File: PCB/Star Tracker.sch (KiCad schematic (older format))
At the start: 29 parts

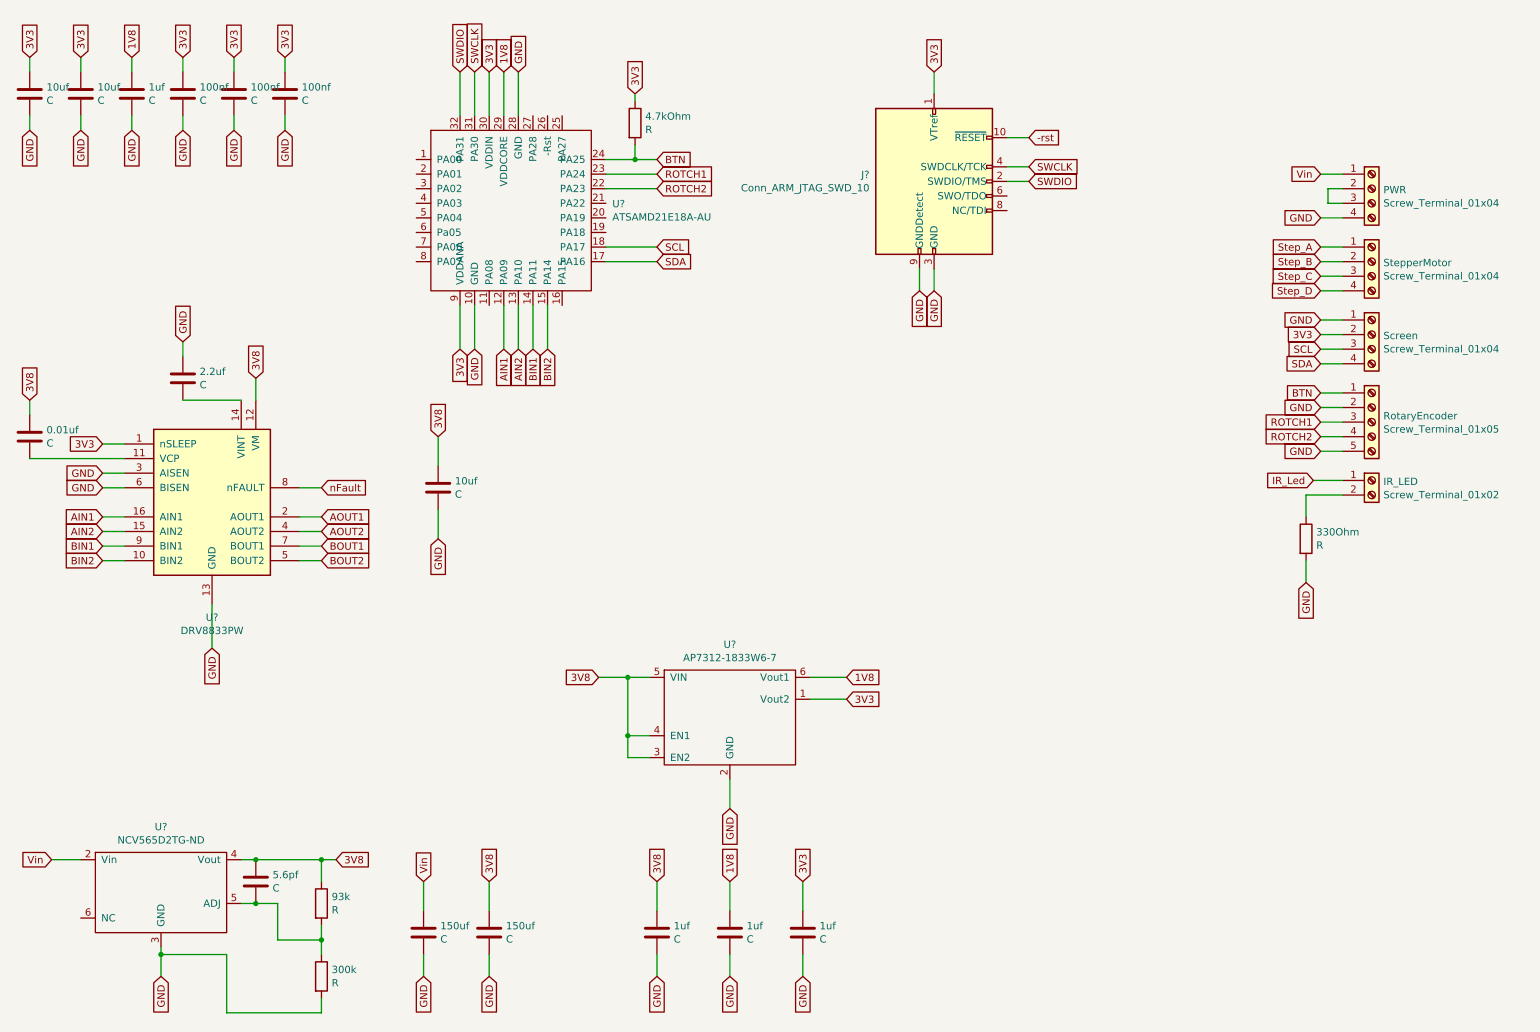
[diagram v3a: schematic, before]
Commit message: Fixed broken schematic and started on layout
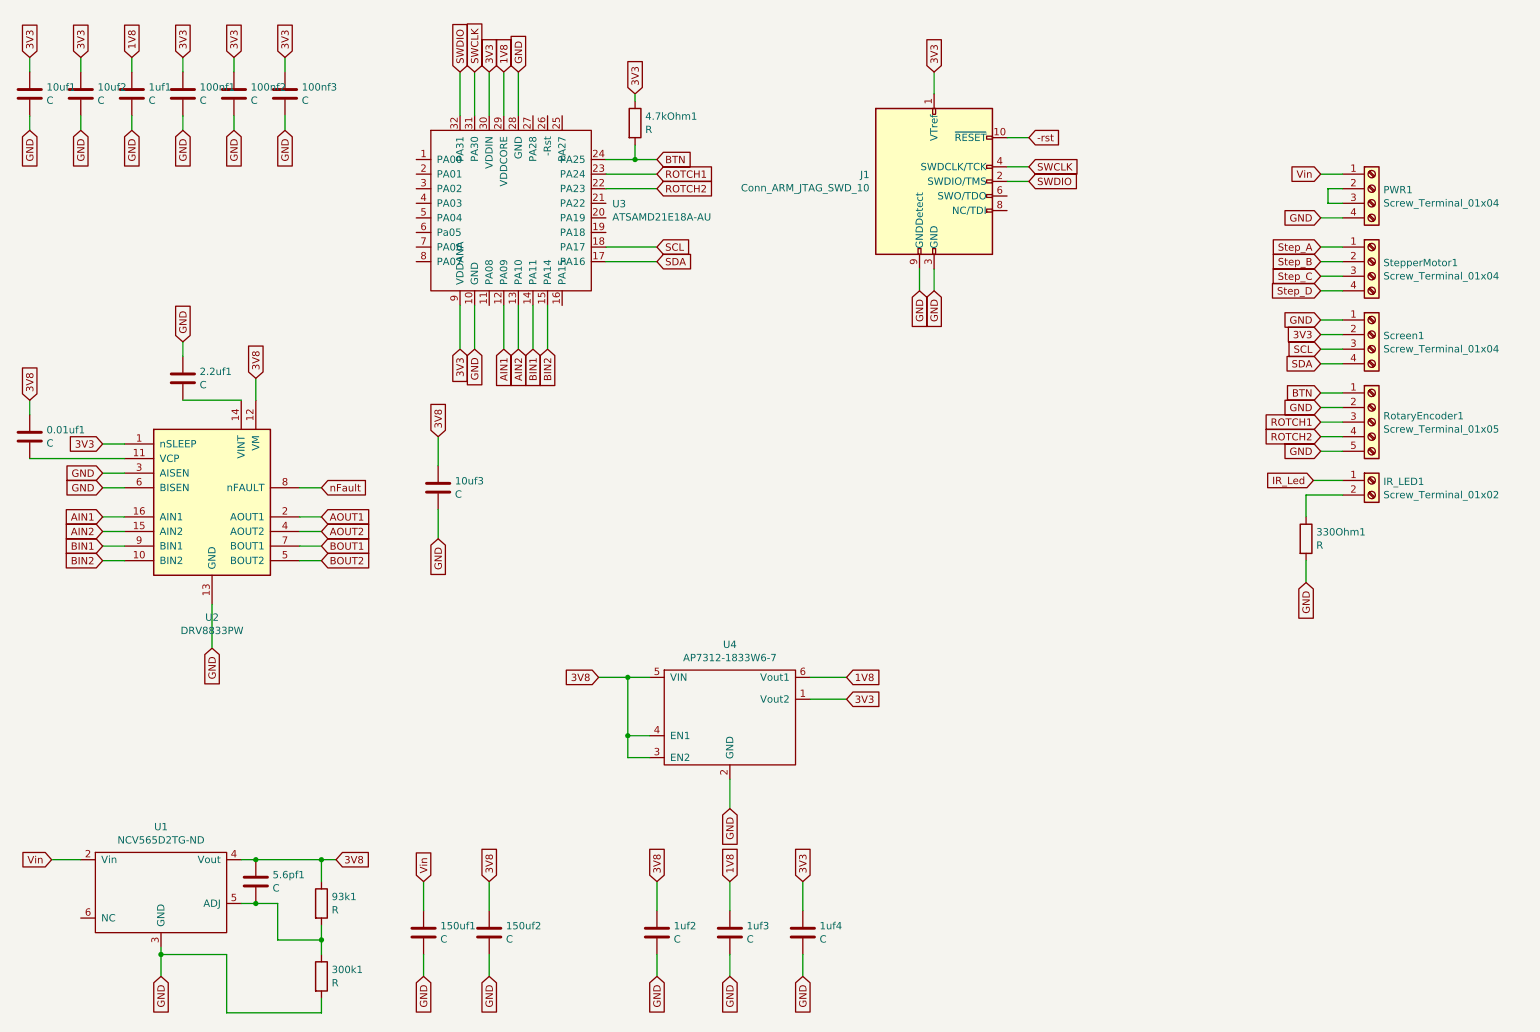
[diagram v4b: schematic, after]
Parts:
- 0.01uf1: renamed from 0.01uf; footprint (none) -> Capacitor_SMD:C_1206_3216Metric
- 100nf1, 100nf2, 100nf3: renamed from 100nf; footprint (none) -> Capacitor_SMD:C_1206_3216Metric
- 10uf1, 10uf2, 10uf3: renamed from 10uf; footprint (none) -> Capacitor_SMD:C_1206_3216Metric
- 150uf1, 150uf2: renamed from 150uf; footprint (none) -> Capacitor_SMD:C_1206_3216Metric
- 1uf1, 1uf2, 1uf3, 1uf4: renamed from 1uf; footprint (none) -> Capacitor_SMD:C_1206_3216Metric
- 2.2uf1: renamed from 2.2uf; footprint (none) -> Capacitor_SMD:C_1206_3216Metric
- 300k1: renamed from 300k; footprint (none) -> Resistor_SMD:R_1206_3216Metric
- 330Ohm1: renamed from 330Ohm; footprint (none) -> Resistor_SMD:R_1206_3216Metric
- 4.7kOhm1: renamed from 4.7kOhm; footprint (none) -> Resistor_SMD:R_1206_3216Metric
- 5.6pf1: renamed from 5.6pf; footprint (none) -> Capacitor_SMD:C_1206_3216Metric
- 93k1: renamed from 93k; footprint (none) -> Resistor_SMD:R_1206_3216Metric
- IR_LED1: renamed from IR_LED; footprint (none) -> Connector_Phoenix_MC:PhoenixContact_MC_1,5_2-G-3.5_1x02_P3.50mm_Horizontal
- J1: renamed from J?; footprint (none) -> Connector_PinHeader_1.27mm:PinHeader_2x05_P1.27mm_Vertical_SMD
- PWR1: renamed from PWR; footprint (none) -> Connector_Phoenix_MC:PhoenixContact_MC_1,5_4-G-3.5_1x04_P3.50mm_Horizontal
- RotaryEncoder1: renamed from RotaryEncoder; footprint (none) -> Connector_Phoenix_MC:PhoenixContact_MC_1,5_5-G-3.5_1x05_P3.50mm_Horizontal
- Screen1: renamed from Screen; footprint (none) -> Connector_Phoenix_MC:PhoenixContact_MC_1,5_4-G-3.5_1x04_P3.50mm_Horizontal
- StepperMotor1: renamed from StepperMotor; footprint (none) -> Connector_Phoenix_MC:PhoenixContact_MC_1,5_4-G-3.5_1x04_P3.50mm_Horizontal
- U1: renamed from U?; footprint (none) -> Package_TO_SOT_SMD:TO-263-5_TabPin6
- U3: renamed from U?; footprint (none) -> Package_QFP:TQFP-32_7x7mm_P0.8mm
- U4: renamed from U?; footprint (none) -> Package_TO_SOT_SMD:SOT-23-6_Handsoldering
- gave numbers to parts that had none: 1

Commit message: Finished layout, minus copper fills
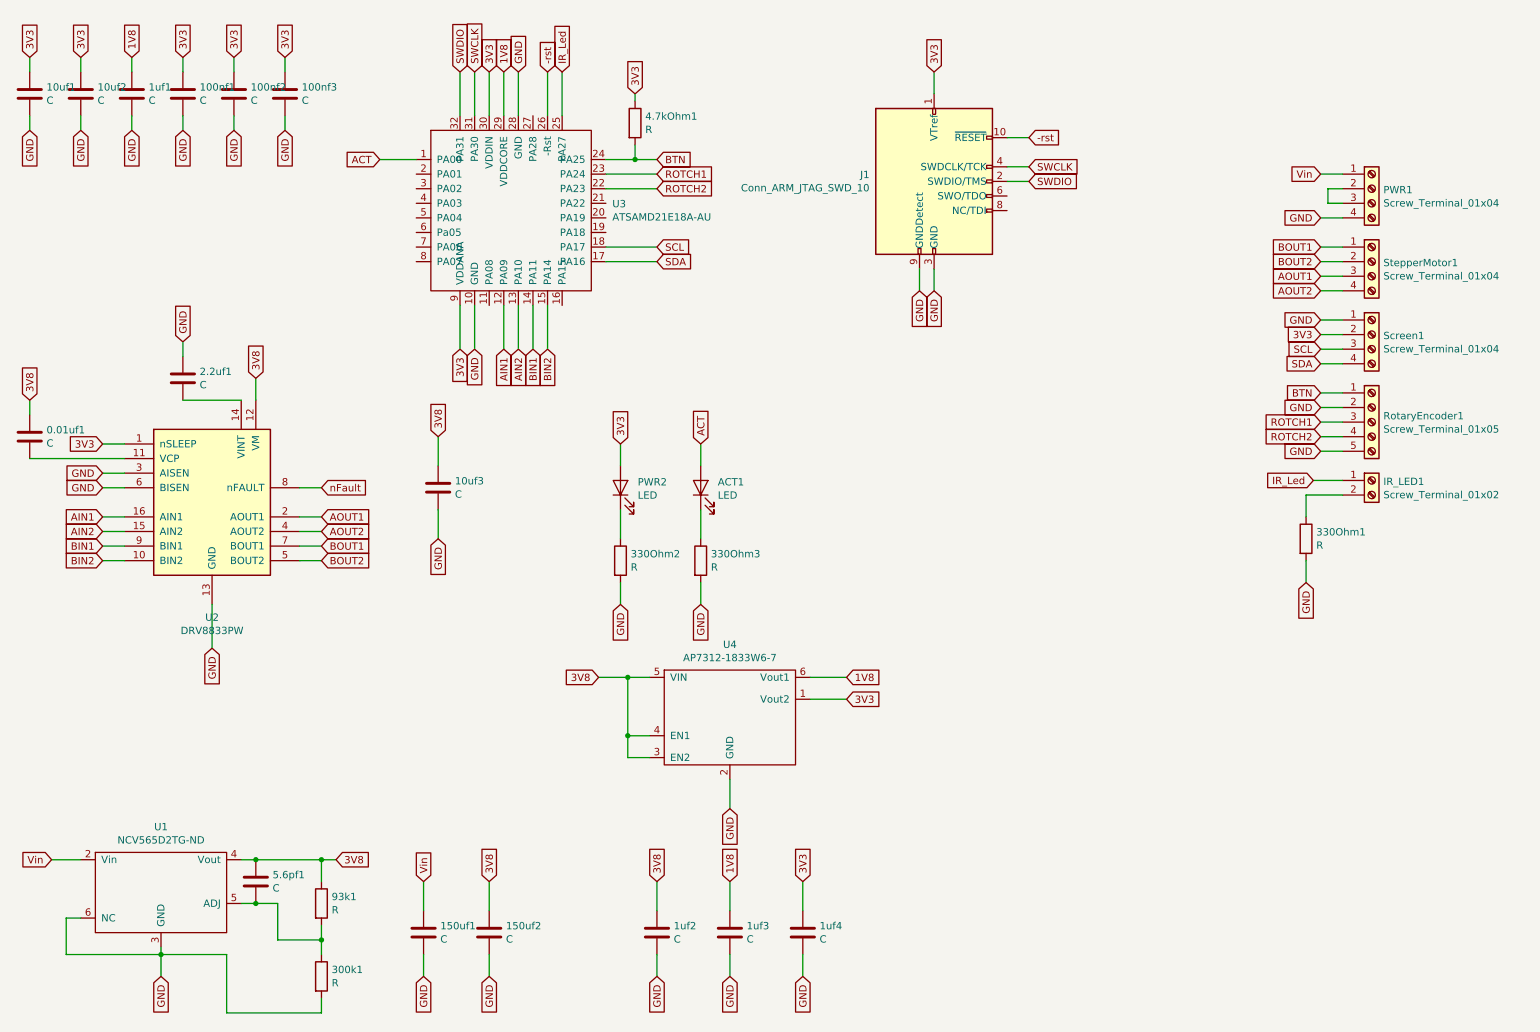
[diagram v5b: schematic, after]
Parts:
- added 330Ohm2, 330Ohm3: R, Resistor_SMD:R_1206_3216Metric_Pad1.42x1.75mm_HandSolder, symbol Device:R
- added ACT1, PWR2: LED, Diode_SMD:D_1206_3216Metric_Pad1.42x1.75mm_HandSolder, symbol Device:LED
- 0.01uf1, 100nf1, 100nf2, 100nf3, 10uf1, 10uf2, 10uf3, 150uf1, 150uf2, 1uf1, 1uf2, 1uf3, 1uf4, 2.2uf1, 5.6pf1: footprint Capacitor_SMD:C_1206_3216Metric -> Capacitor_SMD:C_1206_3216Metric_Pad1.42x1.75mm_HandSolder
- 300k1, 330Ohm1, 4.7kOhm1, 93k1: footprint Resistor_SMD:R_1206_3216Metric -> Resistor_SMD:R_1206_3216Metric_Pad1.42x1.75mm_HandSolder
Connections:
- net Step_A is gone; now on net BOUT1: StepperMotor1.1 (Pin_1)
- net Step_B is gone; now on net BOUT2: StepperMotor1.2 (Pin_2)
- net Step_C is gone; now on net AOUT1: StepperMotor1.3 (Pin_3)
- net Step_D is gone; now on net AOUT2: StepperMotor1.4 (Pin_4)
- net -rst: now also U3.26 (-Rst)
- net 3V3: now also PWR2.2 (A)
- net GND: now also U1.6 (NC), 330Ohm2.2, 330Ohm3.2
- net IR_Led: now also U3.25 (PA27)
- net ACT: now reaches U3.1 (PA00)
- net ACT: now also ACT1.2 (A)
- new net: 330Ohm2.1, PWR2.1 (K)
- new net: 330Ohm3.1, ACT1.1 (K)
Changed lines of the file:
@@
 EESchema Schematic File Version 4
 LIBS:power
-LIBS:device
 LIBS:74xx
-LIBS:audio
-LIBS:interface
 LIBS:Star Tracker-cache
 EELAYER 30 0
@@
 F 0 "100nf3" H 2565 1096 50  0000 L CNN
 F 1 "C" H 2565 1005 50  0000 L CNN
-F 2 "Capacitor_SMD:C_1206_3216Metric" H 2488 900 50  0001 C CNN
+F 2 "Capacitor_SMD:C_1206_3216Metric_Pad1.42x1.75mm_HandSolder" H 2488 900 50  0001 C CNN
 F 3 "~" H 2450 1050 50  0001 C CNN
 	1    2450 1050
@@
 F 0 "100nf2" H 2215 1096 50  0000 L CNN
 F 1 "C" H 2215 1005 50  0000 L CNN
-F 2 "Capacitor_SMD:C_1206_3216Metric" H 2138 900 50  0001 C CNN
+F 2 "Capacitor_SMD:C_1206_3216Metric_Pad1.42x1.75mm_HandSolder" H 2138 900 50  0001 C CNN
 F 3 "~" H 2100 1050 50  0001 C CNN
 	1    2100 1050
@@
 F 0 "100nf1" H 1865 1096 50  0000 L CNN
 F 1 "C" H 1865 1005 50  0000 L CNN
-F 2 "Capacitor_SMD:C_1206_3216Metric" H 1788 900 50  0001 C CNN
+F 2 "Capacitor_SMD:C_1206_3216Metric_Pad1.42x1.75mm_HandSolder" H 1788 900 50  0001 C CNN
 F 3 "~" H 1750 1050 50  0001 C CNN
 	1    1750 1050
@@
 F 0 "1uf1" H 1515 1096 50  0000 L CNN
 F 1 "C" H 1515 1005 50  0000 L CNN
-F 2 "Capacitor_SMD:C_1206_3216Metric" H 1438 900 50  0001 C CNN
+F 2 "Capacitor_SMD:C_1206_3216Metric_Pad1.42x1.75mm_HandSolder" H 1438 900 50  0001 C CNN
 F 3 "~" H 1400 1050 50  0001 C CNN
 	1    1400 1050
@@
 F 0 "10uf2" H 1165 1096 50  0000 L CNN
 F 1 "C" H 1165 1005 50  0000 L CNN
-F 2 "Capacitor_SMD:C_1206_3216Metric" H 1088 900 50  0001 C CNN
+F 2 "Capacitor_SMD:C_1206_3216Metric_Pad1.42x1.75mm_HandSolder" H 1088 900 50  0001 C CNN
 F 3 "~" H 1050 1050 50  0001 C CNN
 	1    1050 1050
@@
 F 0 "10uf1" H 815 1096 50  0000 L CNN
 F 1 "C" H 815 1005 50  0000 L CNN
-F 2 "Capacitor_SMD:C_1206_3216Metric" H 738 900 50  0001 C CNN
+F 2 "Capacitor_SMD:C_1206_3216Metric_Pad1.42x1.75mm_HandSolder" H 738 900 50  0001 C CNN
 F 3 "~" H 700 1050 50  0001 C CNN
 	1    700  1050
@@
 	1    0    0    -1
 $EndComp
-$Comp
-L Star_Tracker_Components:NCV565D2TG-ND U1
-U 1 1 5D8BDB71
-P 1600 6450
-F 0 "U1" H 1600 6825 50  0000 C CNN
-F 1 "NCV565D2TG-ND" H 1600 6734 50  0000 C CNN
-F 2 "Package_TO_SOT_SMD:TO-263-5_TabPin6" H 1600 6450 50  0001 C CNN
-F 3 "" H 1600 6450 50  0001 C CNN
-	1    1600 6450
-	1    0    0    -1
-$EndComp
 Text GLabel 850  6300 0    50   Input ~ 0
 Vin
@@
 Wire Wire Line
 	1050 6300 850  6300
-Wire Wire Line
-	1600 6900 1600 6950
 Wire Wire Line
 	2150 6300 2250 6300
@@
 F 0 "93k1" H 2770 6646 50  0000 L CNN
 F 1 "R" H 2770 6555 50  0000 L CNN
-F 2 "Resistor_SMD:R_1206_3216Metric" V 2630 6600 50  0001 C CNN
+F 2 "Resistor_SMD:R_1206_3216Metric_Pad1.42x1.75mm_HandSolder" V 2630 6600 50  0001 C CNN
 F 3 "~" H 2700 6600 50  0001 C CNN
 	1    2700 6600
@@
 F 0 "300k1" H 2770 7146 50  0000 L CNN
 F 1 "R" H 2770 7055 50  0000 L CNN
-F 2 "Resistor_SMD:R_1206_3216Metric" V 2630 7100 50  0001 C CNN
+F 2 "Resistor_SMD:R_1206_3216Metric_Pad1.42x1.75mm_HandSolder" V 2630 7100 50  0001 C CNN
 F 3 "~" H 2700 7100 50  0001 C CNN
 	1    2700 7100
@@
 Wire Wire Line
 	2050 6950 1600 6950
-Connection ~ 1600 6950
 Wire Wire Line
 	1600 6950 1600 7100
@@
 F 0 "5.6pf1" H 2365 6496 50  0000 L CNN
 F 1 "C" H 2365 6405 50  0000 L CNN
-F 2 "Capacitor_SMD:C_1206_3216Metric" H 2288 6300 50  0001 C CNN
+F 2 "Capacitor_SMD:C_1206_3216Metric_Pad1.42x1.75mm_HandSolder" H 2288 6300 50  0001 C CNN
 F 3 "~" H 2250 6450 50  0001 C CNN
 	1    2250 6450
@@
 F 0 "150uf1" H 3515 6846 50  0000 L CNN
 F 1 "C" H 3515 6755 50  0000 L CNN
-F 2 "Capacitor_SMD:C_1206_3216Metric" H 3438 6650 50  0001 C CNN
+F 2 "Capacitor_SMD:C_1206_3216Metric_Pad1.42x1.75mm_HandSolder" H 3438 6650 50  0001 C CNN
 F 3 "~" H 3400 6800 50  0001 C CNN
 	1    3400 6800
@@
 F 0 "150uf2" H 3965 6846 50  0000 L CNN
 F 1 "C" H 3965 6755 50  0000 L CNN
-F 2 "Capacitor_SMD:C_1206_3216Metric" H 3888 6650 50  0001 C CNN
+F 2 "Capacitor_SMD:C_1206_3216Metric_Pad1.42x1.75mm_HandSolder" H 3888 6650 50  0001 C CNN
 F 3 "~" H 3850 6800 50  0001 C CNN
 	1    3850 6800
@@
 F 0 "1uf2" H 5115 6846 50  0000 L CNN
 F 1 "C" H 5115 6755 50  0000 L CNN
-F 2 "Capacitor_SMD:C_1206_3216Metric" H 5038 6650 50  0001 C CNN
+F 2 "Capacitor_SMD:C_1206_3216Metric_Pad1.42x1.75mm_HandSolder" H 5038 6650 50  0001 C CNN
 F 3 "~" H 5000 6800 50  0001 C CNN
 	1    5000 6800
@@
 F 0 "1uf3" H 5615 6846 50  0000 L CNN
 F 1 "C" H 5615 6755 50  0000 L CNN
-F 2 "Capacitor_SMD:C_1206_3216Metric" H 5538 6650 50  0001 C CNN
+F 2 "Capacitor_SMD:C_1206_3216Metric_Pad1.42x1.75mm_HandSolder" H 5538 6650 50  0001 C CNN
 F 3 "~" H 5500 6800 50  0001 C CNN
 	1    5500 6800
@@
 F 0 "1uf4" H 6115 6846 50  0000 L CNN
 F 1 "C" H 6115 6755 50  0000 L CNN
-F 2 "Capacitor_SMD:C_1206_3216Metric" H 6038 6650 50  0001 C CNN
+F 2 "Capacitor_SMD:C_1206_3216Metric_Pad1.42x1.75mm_HandSolder" H 6038 6650 50  0001 C CNN
 F 3 "~" H 6000 6800 50  0001 C CNN
 	1    6000 6800
@@
 	9550 2900 9700 2900
 Text GLabel 9550 2100 0    50   Input ~ 0
-Step_A
+BOUT1
 Text GLabel 9550 2200 0    50   Input ~ 0
-Step_B
+BOUT2
 Text GLabel 9550 2300 0    50   Input ~ 0
-Step_C
+AOUT1
 Text GLabel 9550 2400 0    50   Input ~ 0
-Step_D
+AOUT2
 $Comp
 L Connector:Screw_Terminal_01x02 IR_LED1
@@
 F 0 "0.01uf1" H 815 3446 50  0000 L CNN
 F 1 "C" H 815 3355 50  0000 L CNN
-F 2 "Capacitor_SMD:C_1206_3216Metric" H 738 3250 50  0001 C CNN
+F 2 "Capacitor_SMD:C_1206_3216Metric_Pad1.42x1.75mm_HandSolder" H 738 3250 50  0001 C CNN
 F 3 "~" H 700 3400 50  0001 C CNN
 	1    700  3400
@@
 F 0 "2.2uf1" H 1865 3046 50  0000 L CNN
 F 1 "C" H 1865 2955 50  0000 L CNN
-F 2 "Capacitor_SMD:C_1206_3216Metric" H 1788 2850 50  0001 C CNN
+F 2 "Capacitor_SMD:C_1206_3216Metric_Pad1.42x1.75mm_HandSolder" H 1788 2850 50  0001 C CNN
 F 3 "~" H 1750 3000 50  0001 C CNN
 	1    1750 3000
@@
 F 0 "10uf3" H 3615 3796 50  0000 L CNN
 F 1 "C" H 3615 3705 50  0000 L CNN
-F 2 "Capacitor_SMD:C_1206_3216Metric" H 3538 3600 50  0001 C CNN
+F 2 "Capacitor_SMD:C_1206_3216Metric_Pad1.42x1.75mm_HandSolder" H 3538 3600 50  0001 C CNN
 F 3 "~" H 3500 3750 50  0001 C CNN
 	1    3500 3750
@@
 F 0 "330Ohm1" H 9520 4146 50  0000 L CNN
 F 1 "R" H 9520 4055 50  0000 L CNN
-F 2 "Resistor_SMD:R_1206_3216Metric" V 9380 4100 50  0001 C CNN
+F 2 "Resistor_SMD:R_1206_3216Metric_Pad1.42x1.75mm_HandSolder" V 9380 4100 50  0001 C CNN
 F 3 "~" H 9450 4100 50  0001 C CNN
 	1    9450 4100
@@
 F 0 "4.7kOhm1" H 4920 1296 50  0000 L CNN
 F 1 "R" H 4920 1205 50  0000 L CNN
-F 2 "Resistor_SMD:R_1206_3216Metric" V 4780 1250 50  0001 C CNN
+F 2 "Resistor_SMD:R_1206_3216Metric_Pad1.42x1.75mm_HandSolder" V 4780 1250 50  0001 C CNN
 F 3 "~" H 4850 1250 50  0001 C CNN
 	1    4850 1250
@@
 Wire Wire Line
 	5000 1700 4650 1700
+$Comp
+L Star_Tracker_Components:NCV565D2TG-ND U1
+U 1 1 5D9549AA
+P 1600 6450
+F 0 "U1" H 1600 6825 50  0000 C CNN
+F 1 "NCV565D2TG-ND" H 1600 6734 50  0000 C CNN
+F 2 "Package_TO_SOT_SMD:TO-263-5_TabPin6" H 1600 6450 50  0001 C CNN
+F 3 "" H 1600 6450 50  0001 C CNN
+	1    1600 6450
+	1    0    0    -1
+$EndComp
+Wire Wire Line
+	1600 6900 1600 6950
+Connection ~ 1600 6950
+Text GLabel 4250 900  1    50   Input ~ 0
+-rst
+Text GLabel 4350 900  1    50   Input ~ 0
+IR_Led
+Wire Wire Line
+	4250 900  4250 1200
+Wire Wire Line
+	4350 900  4350 1200
+Wire Wire Line
+	1050 6700 950  6700
+Wire Wire Line
+	950  6700 950  6950
+Wire Wire Line
+	950  6950 1600 6950
+$Comp
+L Device:LED PWR2
+U 1 1 5DA0AA32
+P 4750 3750
+F 0 "PWR2" V 4789 3632 50  0000 R CNN
+F 1 "LED" V 4698 3632 50  0000 R CNN
+F 2 "Diode_SMD:D_1206_3216Metric_Pad1.42x1.75mm_HandSolder" H 4750 3750 50  0001 C CNN
+F 3 "~" H 4750 3750 50  0001 C CNN
+	1    4750 3750
+	0    -1   -1   0
+$EndComp
+$Comp
+L Device:LED ACT1
+U 1 1 5DA0B6E4
+P 5300 3750
+F 0 "ACT1" V 5339 3633 50  0000 R CNN
+F 1 "LED" V 5248 3633 50  0000 R CNN
+F 2 "Diode_SMD:D_1206_3216Metric_Pad1.42x1.75mm_HandSolder" H 5300 3750 50  0001 C CNN
+F 3 "~" H 5300 3750 50  0001 C CNN
+	1    5300 3750
+	0    -1   -1   0
+$EndComp
+$Comp
+L Device:R 330Ohm2
+U 1 1 5DA0D34E
+P 4750 4250
+F 0 "330Ohm2" H 4820 4296 50  0000 L CNN
+F 1 "R" H 4820 4205 50  0000 L CNN
+F 2 "Resistor_SMD:R_1206_3216Metric_Pad1.42x1.75mm_HandSolder" V 4680 4250 50  0001 C CNN
+F 3 "~" H 4750 4250 50  0001 C CNN
+	1    4750 4250
+	1    0    0    -1
+$EndComp
+$Comp
+L Device:R 330Ohm3
+U 1 1 5DA0DBD9
+P 5300 4250
+F 0 "330Ohm3" H 5370 4296 50  0000 L CNN
+F 1 "R" H 5370 4205 50  0000 L CNN
+F 2 "Resistor_SMD:R_1206_3216Metric_Pad1.42x1.75mm_HandSolder" V 5230 4250 50  0001 C CNN
+F 3 "~" H 5300 4250 50  0001 C CNN
+	1    5300 4250
+	1    0    0    -1
+$EndComp
+Wire Wire Line
+	4750 3900 4750 4100
+Wire Wire Line
+	5300 3900 5300 4100
+Text GLabel 4750 3450 1    50   Input ~ 0
+3V3
+Text GLabel 5300 3450 1    50   Input ~ 0
+ACT
+Text GLabel 4750 4550 3    50   Input ~ 0
+GND
+Text GLabel 5300 4550 3    50   Input ~ 0
+GND
+Wire Wire Line
+	4750 3450 4750 3600
+Wire Wire Line
+	5300 3450 5300 3600
+Wire Wire Line
+	4750 4400 4750 4550
+Wire Wire Line
+	5300 4400 5300 4550
+Text GLabel 3100 1500 0    50   Input ~ 0
+ACT
+Wire Wire Line
+	3350 1500 3100 1500
 $EndSCHEMATC
